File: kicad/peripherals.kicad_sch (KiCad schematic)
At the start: 38 parts, among them J3 GNSS Antenna, J4 RF Antenna, J5 NSIM-5-B, Q1 SS8050, Q2 SS8050, Q3 SS8050, U2 SIM7080G, U3 TXB0108RGY

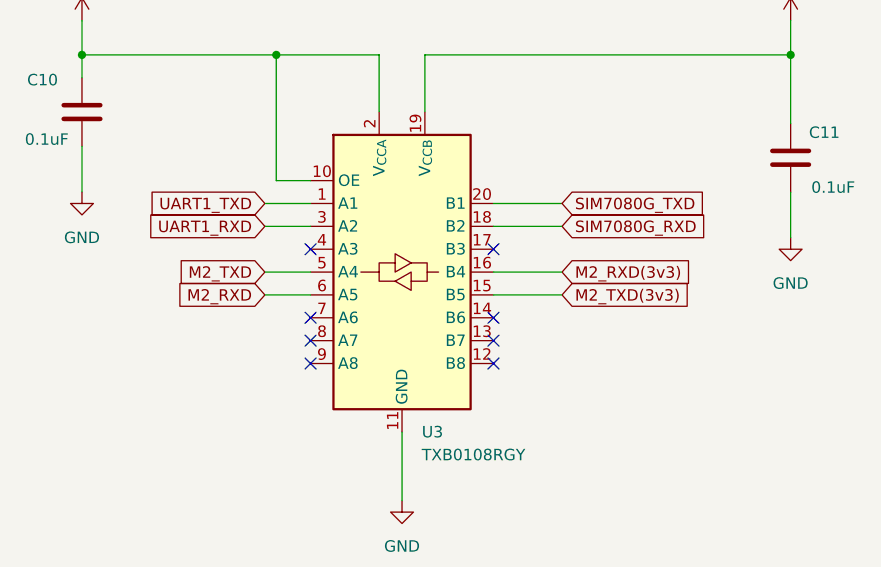
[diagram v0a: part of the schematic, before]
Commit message: Update level shifter schematic
Signed-off-by: JeffMboya <jangina.mboya@gmail.com>
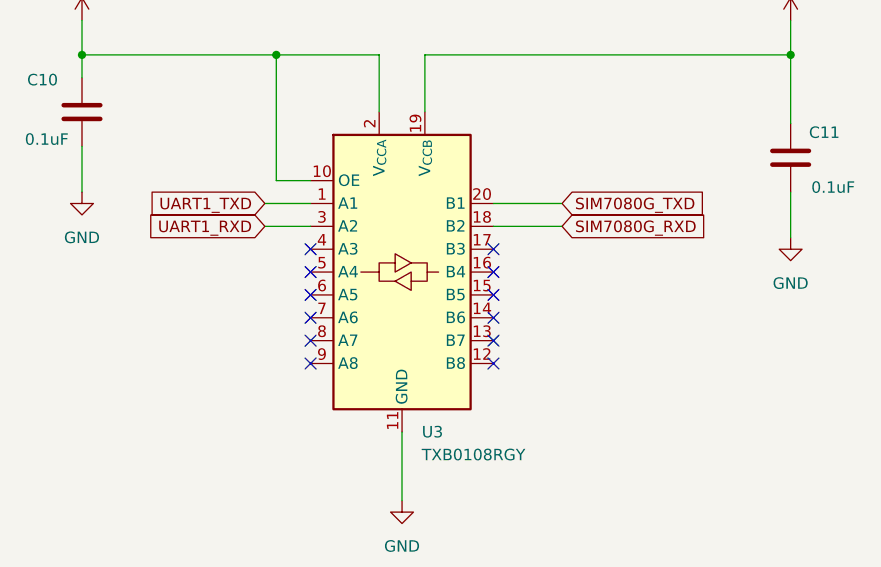
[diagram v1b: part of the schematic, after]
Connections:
- net M2_RXD: no longer names the net of U3.6 (A5)
- net M2_RXD(3v3): no longer names the net of U3.16 (B4)
- net M2_TXD: no longer names the net of U3.5 (A4)
- net M2_TXD(3v3): no longer names the net of U3.15 (B5)
- no-connect marks 38 -> 42
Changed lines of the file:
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@@
 		(rev "v0.1.0")
 		(company "Abstract Machines")
-		(comment 1 "Designed By: Rodney Osodo")
+		(comment 1 "Designed By: Jeff Mboya")
 		(comment 2 "Approved By:")
 	)
@@
 	)
 	(no_connect
+		(at 81.28 92.71)
+	)
+	(no_connect
 		(at 81.28 80.01)
 	)
@@
 	)
 	(no_connect
+		(at 336.55 153.67)
+	)
+	(no_connect
+		(at 336.55 151.13)
+	)
+	(no_connect
 		(at 356.87 161.29)
 	)
@@
 	)
 	(no_connect
+		(at 356.87 151.13)
+	)
+	(no_connect
 		(at 356.87 218.44)
 	)
 	(no_connect
-		(at 81.28 92.71)
-	)
-	(no_connect
 		(at 132.08 90.17)
 	)
@@
 	)
 	(no_connect
+		(at 356.87 153.67)
+	)
+	(no_connect
 		(at 132.08 100.33)
 	)
@@
 	(wire
 		(pts
-			(xy 331.47 151.13) (xy 336.55 151.13)
-		)
-		(stroke
-			(width 0)
-			(type default)
-		)
-	)
-	(wire
-		(pts
 			(xy 142.24 62.23) (xy 132.08 62.23)
 		)
@@
 	(wire
 		(pts
-			(xy 364.49 151.13) (xy 356.87 151.13)
-		)
-		(stroke
-			(width 0)
-			(type default)
-		)
-	)
-	(wire
-		(pts
 			(xy 331.47 146.05) (xy 336.55 146.05)
 		)
@@
 	(wire
 		(pts
-			(xy 364.49 153.67) (xy 356.87 153.67)
-		)
-		(stroke
-			(width 0)
-			(type default)
-		)
-	)
-	(wire
-		(pts
 			(xy 132.08 153.67) (xy 132.08 156.21)
 		)
@@
 		(pts
 			(xy 180.34 261.62) (xy 180.34 255.27)
-		)
-		(stroke
-			(width 0)
-			(type default)
-		)
-	)
-	(wire
-		(pts
-			(xy 331.47 153.67) (xy 336.55 153.67)
 		)
 		(stroke
@@
 		)
 	)
-	(global_label "M2_TXD(3v3)"
-		(shape input)
-		(at 364.49 153.67 0)
-		(fields_autoplaced yes)
-		(effects
-			(font
-				(size 1.27 1.27)
-			)
-			(justify left)
-		)
-		(property "Intersheetrefs" "${INTERSHEET_REFS}"
-			(at 379.6308 153.67 0)
-			(effects
-				(font
-					(size 1.27 1.27)
-				)
-				(justify left)
-				(hide yes)
-			)
-		)
-	)
 	(global_label "SIM7080G_TXD"
 		(shape input)
@@
 		)
 	)
-	(global_label "M2_TXD"
-		(shape input)
-		(at 331.47 151.13 180)
-		(fields_autoplaced yes)
-		(effects
-			(font
-				(size 1.27 1.27)
-			)
-			(justify right)
-		)
-		(property "Intersheetrefs" "${INTERSHEET_REFS}"
-			(at 321.4092 151.13 0)
-			(effects
-				(font
-					(size 1.27 1.27)
-				)
-				(justify right)
-				(hide yes)
-			)
-		)
-	)
-	(global_label "M2_RXD(3v3)"
-		(shape input)
-		(at 364.49 151.13 0)
-		(fields_autoplaced yes)
-		(effects
-			(font
-				(size 1.27 1.27)
-			)
-			(justify left)
-		)
-		(property "Intersheetrefs" "${INTERSHEET_REFS}"
-			(at 379.9332 151.13 0)
-			(effects
-				(font
-					(size 1.27 1.27)
-				)
-				(justify left)
-				(hide yes)
-			)
-		)
-	)
 	(global_label "SIM7080G_RXD"
 		(shape input)
@@
 			(effects
 				(font
-					(size 1.27 1.27)
-				)
-				(justify right)
-				(hide yes)
-			)
-		)
-	)
-	(global_label "M2_RXD"
-		(shape input)
-		(at 331.47 153.67 180)
-		(fields_autoplaced yes)
-		(effects
-			(font
-				(size 1.27 1.27)
-			)
-			(justify right)
-		)
-		(property "Intersheetrefs" "${INTERSHEET_REFS}"
-			(at 321.1068 153.67 0)
-			(effects
-				(font
